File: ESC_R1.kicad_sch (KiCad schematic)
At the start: 0 parts

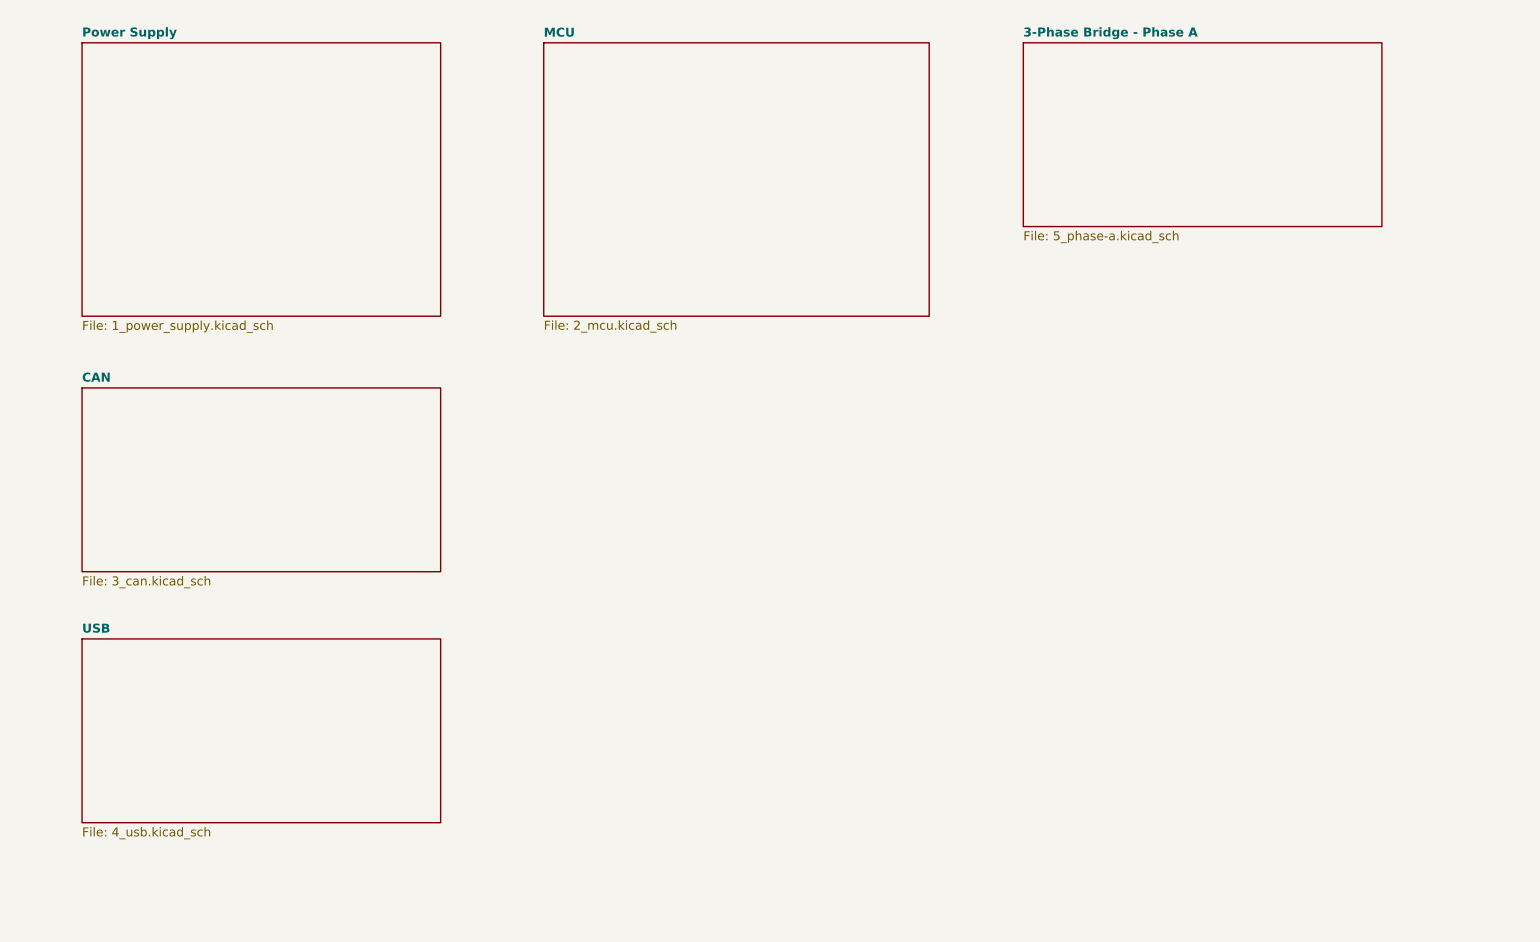
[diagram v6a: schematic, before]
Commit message: feat: new phases, LED pins
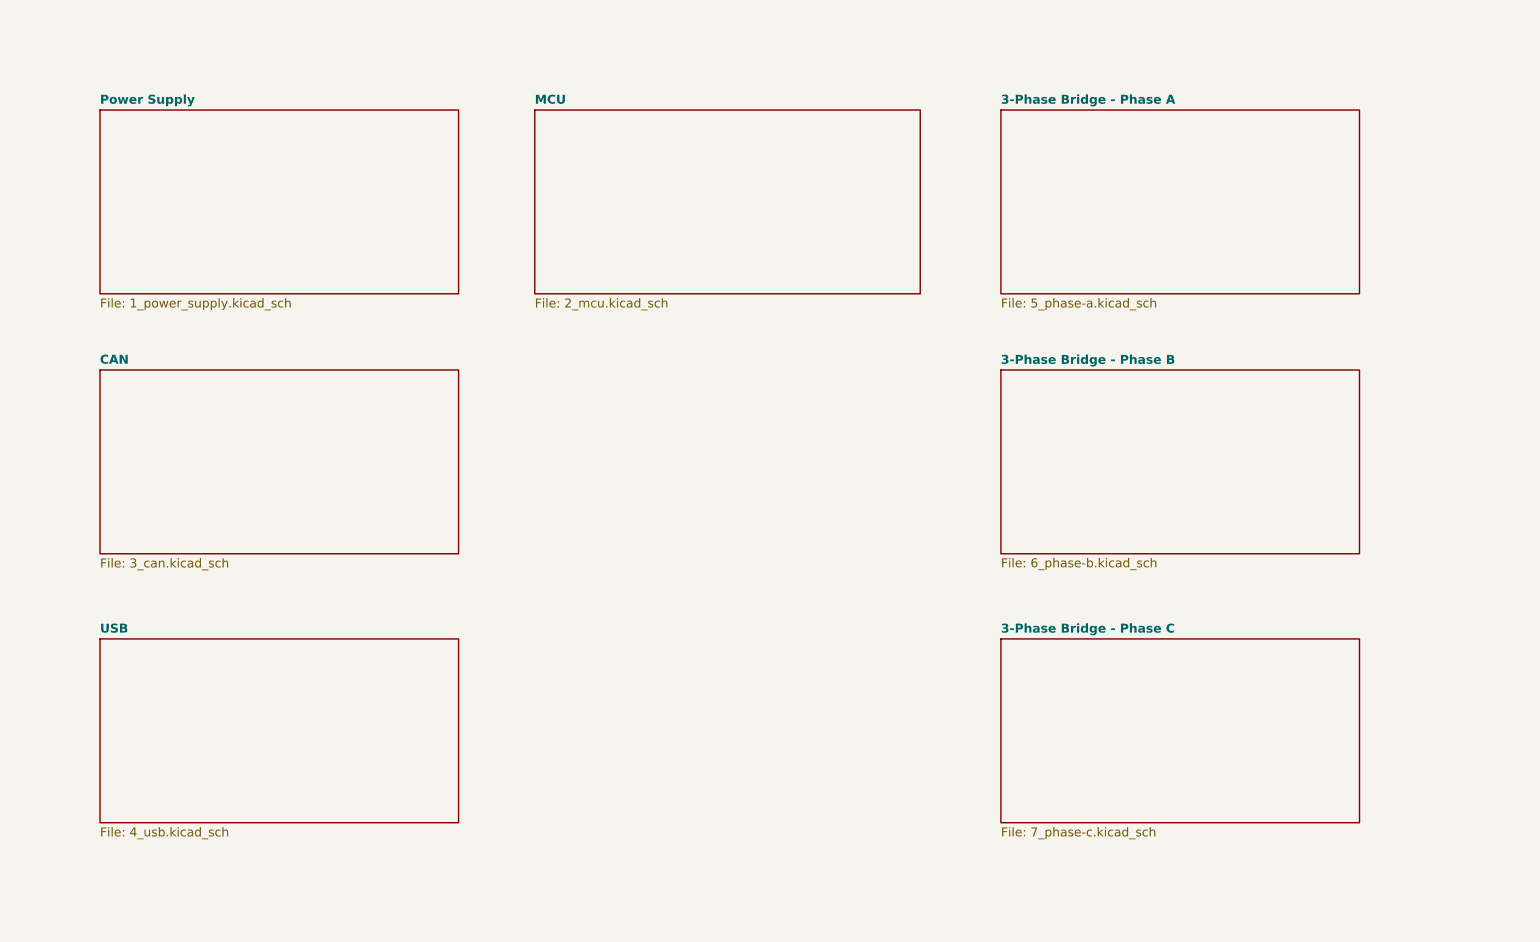
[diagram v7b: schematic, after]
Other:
- added sheet 3-Phase Bridge - Phase B (6_phase-b.kicad_sch)
- added sheet 3-Phase Bridge - Phase C (7_phase-c.kicad_sch)
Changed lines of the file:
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@@
     (rev "1.0")
   )
-  (sheet (at 52.07 122.555) (size 50.8 26.035) (fields_autoplaced)
+  (sheet (at 54.61 122.555) (size 50.8 26.035) (fields_autoplaced)
     (stroke (width 0.2) (type solid))
     (fill (color 0 0 0 0.0000))
-    (property "Sheetname" "USB" (at 52.07 121.8196 0)
+    (property "Sheetname" "USB" (at 54.61 121.8196 0)
       (effects (font (size 1.27 1.27) bold) (justify left bottom))
     )
-    (property "Sheetfile" "4_usb.kicad_sch" (at 52.07 149.1984 0)
+    (property "Sheetfile" "4_usb.kicad_sch" (at 54.61 149.1984 0)
+      (effects (font (size 1.27 1.27)) (justify left top))
+    )
+    (instances
+      (project "ESC_R1"
+        (path "/9dea2e18-5867-4ed4-a12d-7ee109225de0" (page "4"))
+      )
+    )
+  )
+  (sheet (at 116.205 47.625) (size 54.61 26.035) (fields_autoplaced)
+    (stroke (width 0.2) (type solid))
+    (fill (color 0 0 0 0.0000))
+    (property "Sheetname" "MCU" (at 116.205 46.8896 0)
+      (effects (font (size 1.27 1.27) bold) (justify left bottom))
+    )
+    (property "Sheetfile" "2_mcu.kicad_sch" (at 116.205 74.2684 0)
+      (effects (font (size 1.27 1.27)) (justify left top))
+    )
+    (instances
+      (project "ESC_R1"
+        (path "/9dea2e18-5867-4ed4-a12d-7ee109225de0" (page "2"))
+      )
+    )
+  )
+  (sheet (at 182.245 122.555) (size 50.8 26.035) (fields_autoplaced)
+    (stroke (width 0.2) (type solid))
+    (fill (color 0 0 0 0.0000))
+    (property "Sheetname" "3-Phase Bridge - Phase C" (at 182.245 121.8196 0)
+      (effects (font (size 1.27 1.27) bold) (justify left bottom))
+    )
+    (property "Sheetfile" "7_phase-c.kicad_sch" (at 182.245 149.1984 0)
+      (effects (font (size 1.27 1.27)) (justify left top))
+    )
+    (instances
+      (project "ESC_R1"
+        (path "/9dea2e18-5867-4ed4-a12d-7ee109225de0" (page "7"))
+      )
+    )
+  )
+  (sheet (at 182.245 47.625) (size 50.8 26.035) (fields_autoplaced)
+    (stroke (width 0.2) (type solid))
+    (fill (color 0 0 0 0.0000))
+    (property "Sheetname" "3-Phase Bridge - Phase A" (at 182.245 46.8896 0)
+      (effects (font (size 1.27 1.27) bold) (justify left bottom))
+    )
+    (property "Sheetfile" "5_phase-a.kicad_sch" (at 182.245 74.2684 0)
       (effects (font (size 1.27 1.27)) (justify left top))
     )
@@
     )
   )
-  (sheet (at 117.475 38.1) (size 54.61 38.735) (fields_autoplaced)
+  (sheet (at 54.61 84.455) (size 50.8 26.035) (fields_autoplaced)
     (stroke (width 0.2) (type solid))
     (fill (color 0 0 0 0.0000))
-    (property "Sheetname" "MCU" (at 117.475 37.3884 0)
+    (property "Sheetname" "CAN" (at 54.61 83.7196 0)
       (effects (font (size 1.27 1.27) bold) (justify left bottom))
     )
-    (property "Sheetfile" "2_mcu.kicad_sch" (at 117.475 77.4196 0)
-      (effects (font (size 1.27 1.27)) (justify left top))
-    )
-    (instances
-      (project "ESC_R1"
-        (path "/9dea2e18-5867-4ed4-a12d-7ee109225de0" (page "4"))
-      )
-    )
-  )
-  (sheet (at 185.42 38.1) (size 50.8 26.035) (fields_autoplaced)
-    (stroke (width 0.2) (type solid))
-    (fill (color 0 0 0 0.0000))
-    (property "Sheetname" "3-Phase Bridge - Phase A" (at 185.42 37.3646 0)
-      (effects (font (size 1.27 1.27) bold) (justify left bottom))
-    )
-    (property "Sheetfile" "5_phase-a.kicad_sch" (at 185.42 64.7434 0)
-      (effects (font (size 1.27 1.27)) (justify left top))
-    )
-    (instances
-      (project "ESC_R1"
-        (path "/9dea2e18-5867-4ed4-a12d-7ee109225de0" (page "4"))
-      )
-    )
-  )
-  (sheet (at 52.07 86.995) (size 50.8 26.035) (fields_autoplaced)
-    (stroke (width 0.2) (type solid))
-    (fill (color 0 0 0 0.0000))
-    (property "Sheetname" "CAN" (at 52.07 86.2596 0)
-      (effects (font (size 1.27 1.27) bold) (justify left bottom))
-    )
-    (property "Sheetfile" "3_can.kicad_sch" (at 52.07 113.6384 0)
+    (property "Sheetfile" "3_can.kicad_sch" (at 54.61 111.0984 0)
       (effects (font (size 1.27 1.27)) (justify left top))
     )
@@
     )
   )
-  (sheet (at 52.07 38.1) (size 50.8 38.735) (fields_autoplaced)
+  (sheet (at 54.61 47.625) (size 50.8 26.035) (fields_autoplaced)
     (stroke (width 0.2) (type solid))
     (fill (color 0 0 0 0.0000))
-    (property "Sheetname" "Power Supply" (at 52.07 37.3646 0)
+    (property "Sheetname" "Power Supply" (at 54.61 46.8896 0)
       (effects (font (size 1.27 1.27) bold) (justify left bottom))
     )
-    (property "Sheetfile" "1_power_supply.kicad_sch" (at 52.07 77.4434 0)
+    (property "Sheetfile" "1_power_supply.kicad_sch" (at 54.61 74.2684 0)
       (effects (font (size 1.27 1.27)) (justify left top))
     )
     (instances
       (project "ESC_R1"
-        (path "/9dea2e18-5867-4ed4-a12d-7ee109225de0" (page "2"))
+        (path "/9dea2e18-5867-4ed4-a12d-7ee109225de0" (page "1"))
       )
     )
+  )
+  (sheet (at 182.245 84.455) (size 50.8 26.035) (fields_autoplaced)
+    (stroke (width 0.2) (type solid))
+    (fill (color 0 0 0 0.0000))
+    (property "Sheetname" "3-Phase Bridge - Phase B" (at 182.245 83.7434 0)
+      (effects (font (size 1.27 1.27) bold) (justify left bottom))
+    )
+    (property "Sheetfile" "6_phase-b.kicad_sch" (at 182.245 111.0746 0)
+      (effects (font (size 1.27 1.27)) (justify left top))
+    )
+    (instances
+      (project "ESC_R1"
+        (path "/9dea2e18-5867-4ed4-a12d-7ee109225de0" (page "6"))
+      )
+    )
